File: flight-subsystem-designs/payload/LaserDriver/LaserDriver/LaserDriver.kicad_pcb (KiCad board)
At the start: 4 copper layers, 71 x 71 mm, 54 parts, among them J1 Laser 0, J2 Laser 1, J3 Input, J4 BNC, J6 VIN Pin Header, U1 MAX3967AETG+, U2 DPC6137, U3 MAX3967AETG+, U4 74LVC1G04, U5 SY100ELT22ZG-TR, U6 LDL212PV33R, U7 UCC33420RAQR

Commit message: laserdriver: finish routing (we're so back)
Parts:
- added J5: VIN Banana, Connector:Banana_Jack_1Pin, F.Cu at (145.0, 100.9)
- added J7: GND Banana, Connector:Banana_Jack_1Pin, F.Cu at (160.0, 100.9)
- moved J6 127.8 mm to (151.4, 108.7), turned to 90 degrees
- moved C9 120.3 mm to (127.3, 84.1), turned to -90 degrees
- moved C7 118.1 mm to (140.9, 85.5), turned to 90 degrees
- moved J1 116.4 mm to (190.5, 85.8), turned to 180 degrees
- moved U7 114.4 mm to (134.1, 84.8), turned to 180 degrees
- moved C10 112.7 mm to (125.7, 84.0), turned to -90 degrees
- moved D1 111.8 mm to (142.8, 91.4)
- moved C8 109.8 mm to (142.6, 85.5), turned to 90 degrees
- moved U6 108.0 mm to (123.4, 80.4), turned to -90 degrees
- moved C6 104.8 mm to (123.4, 84.1), turned to -90 degrees
- moved R15 104.4 mm to (141.9, 88.3), turned to 180 degrees
- moved R9 103.7 mm to (159.4, 77.9), turned to 180 degrees
- moved JP6 102.5 mm to (172.6, 92.2), turned to 90 degrees
- moved R14 102.1 mm to (172.7, 82.8)
- moved C5 101.4 mm to (123.4, 77.3)
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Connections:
- C10 pad 1: /Power Input and Filtering/ISO_VIN -> +5V
- C9 pad 1: /Power Input and Filtering/ISO_VIN -> +5V
- U5 pad 7: /SIGNAL_IN -> /ISO_SIGNAL_IN
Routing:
- net GND: track 0.00 -> 47.4 mm, vias 0 -> 53
- net /SIGNAL_IN: track 0.00 -> 43.6 mm
- net /Power Input and Filtering/RAW_GND: track 0.00 -> 38.2 mm
- net /Laser0_PECL_P: track 0.00 -> 33.4 mm
- net /Laser0_PECL_N: track 0.00 -> 33.4 mm
- net +5V: track 0.00 -> 27.2 mm
- net /Laser1_PECL_N: track 0.00 -> 22.9 mm
- net /Laser1_PECL_P: track 0.00 -> 22.5 mm
- net +3V3: track 0.00 -> 21.8 mm, vias 0 -> 26
- net Net-(D1-A): track 0.00 -> 20.0 mm
- net /Laser1_PWR_N: track 0.00 -> 15.5 mm
- net /Laser0_PWR_N: track 0.00 -> 15.3 mm
- net /Laser1_PWR_P: track 0.00 -> 14.4 mm
- net /ISO_SIGNAL_IN: track 0.00 -> 13.7 mm
- net /Laser0_PWR_P: track 0.00 -> 13.5 mm
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- added copper zone on F.Cu, net +3V3
- added copper zone on F.Cu, net +5V
- added copper zone on F.Cu, net /Power Input and Filtering/RAW_GND
- added copper zone on F.Cu, net /Power Input and Filtering/VIN
- added copper zone on F.Cu, net GND
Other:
- board size 71 x 71 mm -> 80.9 x 71 mm
- board text added: "5V IN"
- board text added: "Laser 0 (Non-Inverting)"
- board text added: "Laser 1 (Inverting)"
- board text added: "Laser Driver"
- board text added: "R_MODSET"
- board text added: "SIGNAL"
- board text added: "rev 1.1.0, 02.17.26"
- board text removed: "Inverting"
- board text removed: "Non-inverting"
- board text removed: "Prototype Laser Driver"
- board text removed: "R_MODSET Laser 0"
- board text removed: "R_MODSET Laser 1"
- board text removed: "rev 1.0.0, 02.10.26"

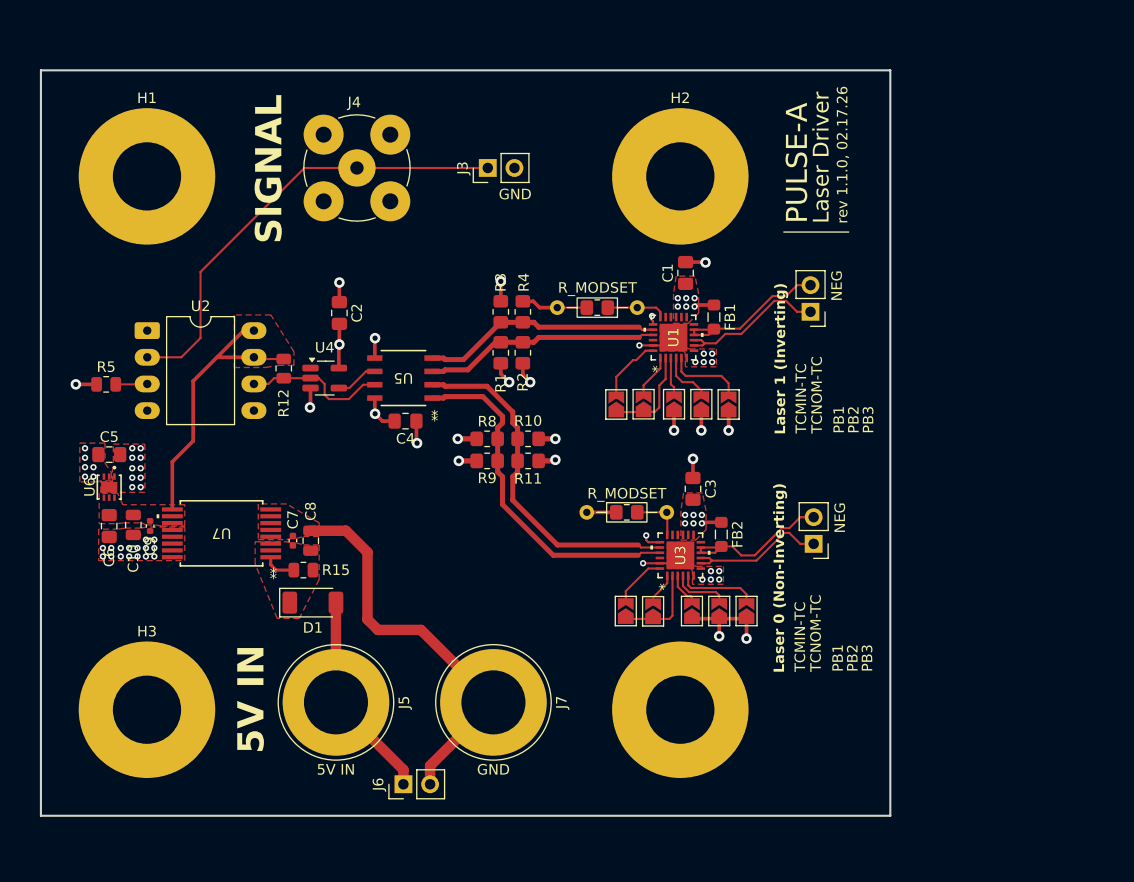
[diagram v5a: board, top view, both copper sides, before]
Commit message: laserdriver: signal gnd isolation; fix drcs; ready to export!
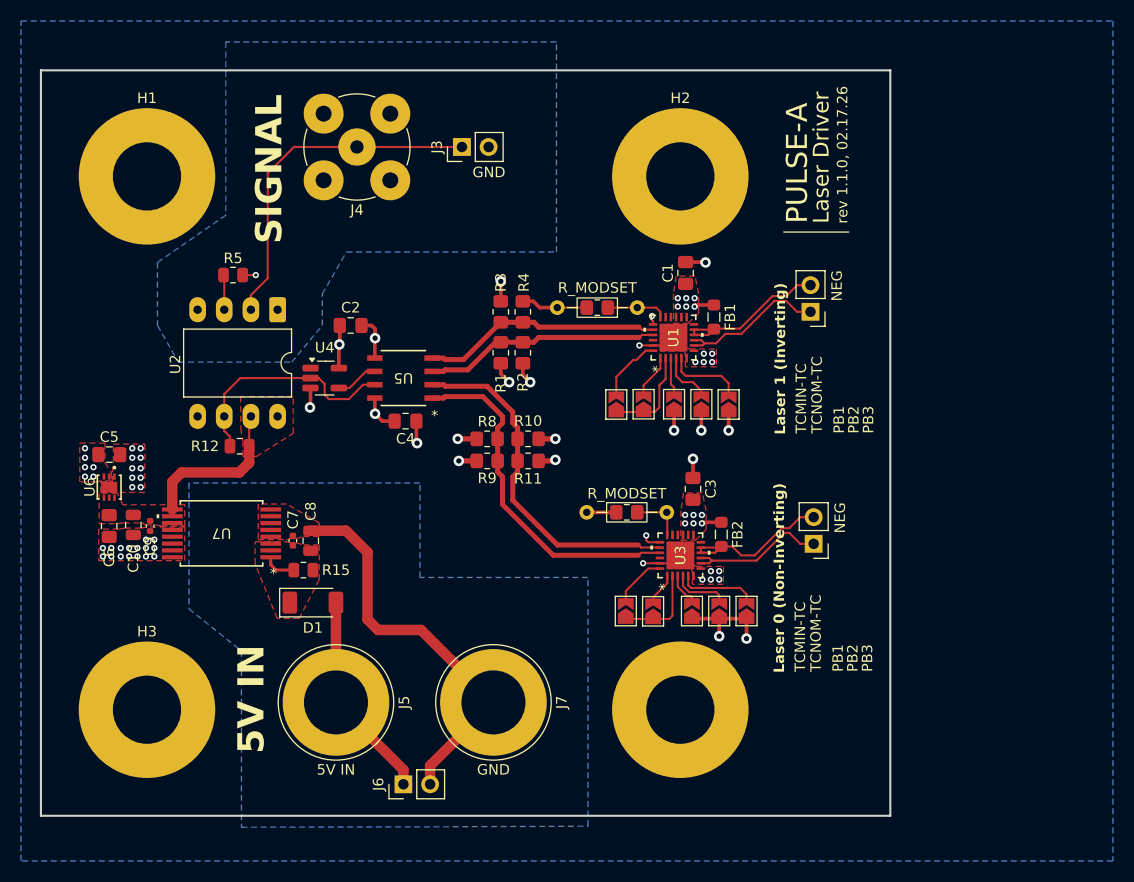
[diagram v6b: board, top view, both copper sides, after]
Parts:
- moved R5 16.0 mm to (135.2, 60.2), turned to 180 degrees
- moved U2 12.6 mm to (139.4, 63.5), turned to -90 degrees
- moved R12 8.50 mm to (135.8, 76.5), turned to 0 degrees
- moved J3 3.17 mm to (157.0, 48.0)
- moved J4 2.00 mm to (147.0, 48.0)
- moved C2 1.60 mm to (146.4, 65.0), turned to 180 degrees
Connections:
- J3 pad 2: GND -> /SIGNAL_GND
- J4 pad 2: GND -> /SIGNAL_GND
- R5 pad 1: GND -> /SIGNAL_GND
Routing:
- net +5V: track 27.2 -> 15.2 mm
- net /SIGNAL_IN: track 43.6 -> 33.2 mm
- net /ISO_SIGNAL_IN: track 13.7 -> 22.2 mm
- net GND: track 47.4 -> 45.9 mm, vias 53 -> 51
- net /SIGNAL_GND: track 0.00 -> 1.25 mm, vias 0 -> 1
- added copper zone on In1.Cu, net /SIGNAL_GND
- added copper zone on B.Cu, net GND
